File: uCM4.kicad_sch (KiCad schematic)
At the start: 77 parts, among them IC1 MAX17048G+, J10 USB_C_Receptacle, J12 Conn_02x08_Odd_Even, J13 Conn_02x07_Odd_Even, J2 Micro_SD_Card_Det, J4 Conn_01x04, J5 DummyJ, J6 DummyJ, J8 Camera 0, J9 Camera 1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

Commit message: Routing
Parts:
- removed TP1, TP3, TP4, TP5, TP6, TP7, TP9: TestPoint, TestPoint:TestPoint_Pad_D1.0mm, symbol Connector:TestPoint
- removed U3: TPD4EUSB30DQAR, Package_SON:USON-10_2.5x1.0mm_P0.5mm, symbol Power_Protection:TPD4EUSB30
- added U5: TPD2EUSB30, Package_TO_SOT_SMD:Texas_DRT-3, symbol Power_Protection:TPD2EUSB30
- J2: footprint CM4:SDCARD_MOLEX_503398-1892 -> Connector_Card:microSD_HC_Hirose_DM3AT-SF-PEJM5
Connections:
- net GND: now also U5.3 (GND)
- net USB_N: now also U5.2 (D-)
- net USB_P: now also U5.1 (D+)
- net ENV_SEL: no longer names the net of Module1.37 (GPIO7)
- no-connect marks 97 -> 96
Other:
- note added: "Might be worth double checking pins one more time."
- note added: "Would be good to double check if this will work as intended."
- moved on the sheet: TP10, TP11, TP12, TP2, TP8

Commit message: Updating LCSC numbers.
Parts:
- C1, C11: LCSC Part # (none) -> C14445
- C2, C3: LCSC Part # (none) -> C1525
- C5: LCSC Part # (none) -> C117956
- C8, C9: LCSC Part # (none) -> C19702
- D1: LCSC Part # (none) -> C181863; LCSC# C181863 -> (none)
- D2: LCSC Part # (none) -> C72043; LCSC# C72043 -> (none)
- D3: LCSC Part # (none) -> C72043
- D8: LCSC Part # (none) -> C727059
- J10: LCSC (none) -> C5184243
- J2: LCSC Part # (none) -> C428492
- J8, J9: LCSC Part # (none) -> C597981
- L1: LCSC Part # (none) -> C19191626
- Module1: LCSC Part # (none) -> C424649; LCSC# C424649 -> (none)
- R10, R13, R15: LCSC Part # (none) -> C21190; LCSC# C21190 -> (none)
- R12, R14: LCSC Part # (none) -> C60490
- R16: LCSC Part # (none) -> C269673
- R29: LCSC Part # (none) -> C25752
- R8, R9: LCSC Part # (none) -> C25905
- SW1: LCSC Part # (none) -> C221907; LCSC# C221911 -> (none)
- SW3: LCSC Part # (none) -> C221907
- U1: LCSC Part # (none) -> C93216
- U18: LCSC Part # (none) -> C250547
- U2: LCSC Part # (none) -> C7829; LCSC# C7829 -> (none)
- U4: LCSC Part # (none) -> C915088
- U5: LCSC Part # (none) -> C3040102
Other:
- note added: "Still need to fix distances for diff pairs"

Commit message: Tuning differential traces and changing some footprints
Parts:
- J2: footprint Connector_Card:microSD_HC_Hirose_DM3AT-SF-PEJM5 -> CM4:SDCARD_MOLEX_503398-1892
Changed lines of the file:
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@@
 			)
 		)
-		(property "Footprint" "Connector_Card:microSD_HC_Hirose_DM3AT-SF-PEJM5"
+		(property "Footprint" "CM4:SDCARD_MOLEX_503398-1892"
 			(at 326.39 38.1 0)
 			(effects

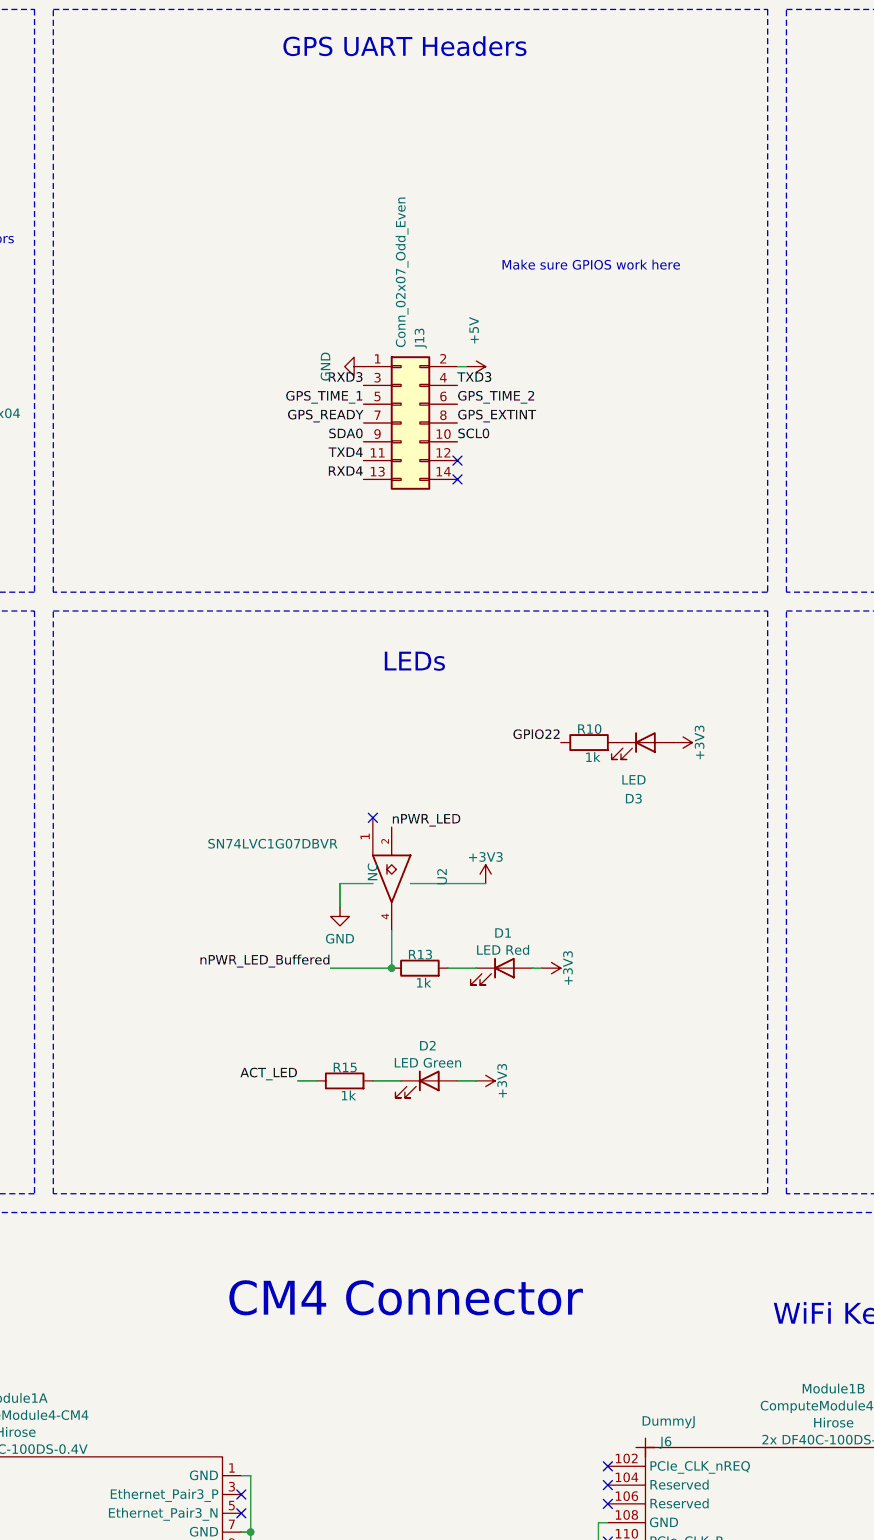
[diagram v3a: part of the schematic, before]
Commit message: Finalized LCSC selections
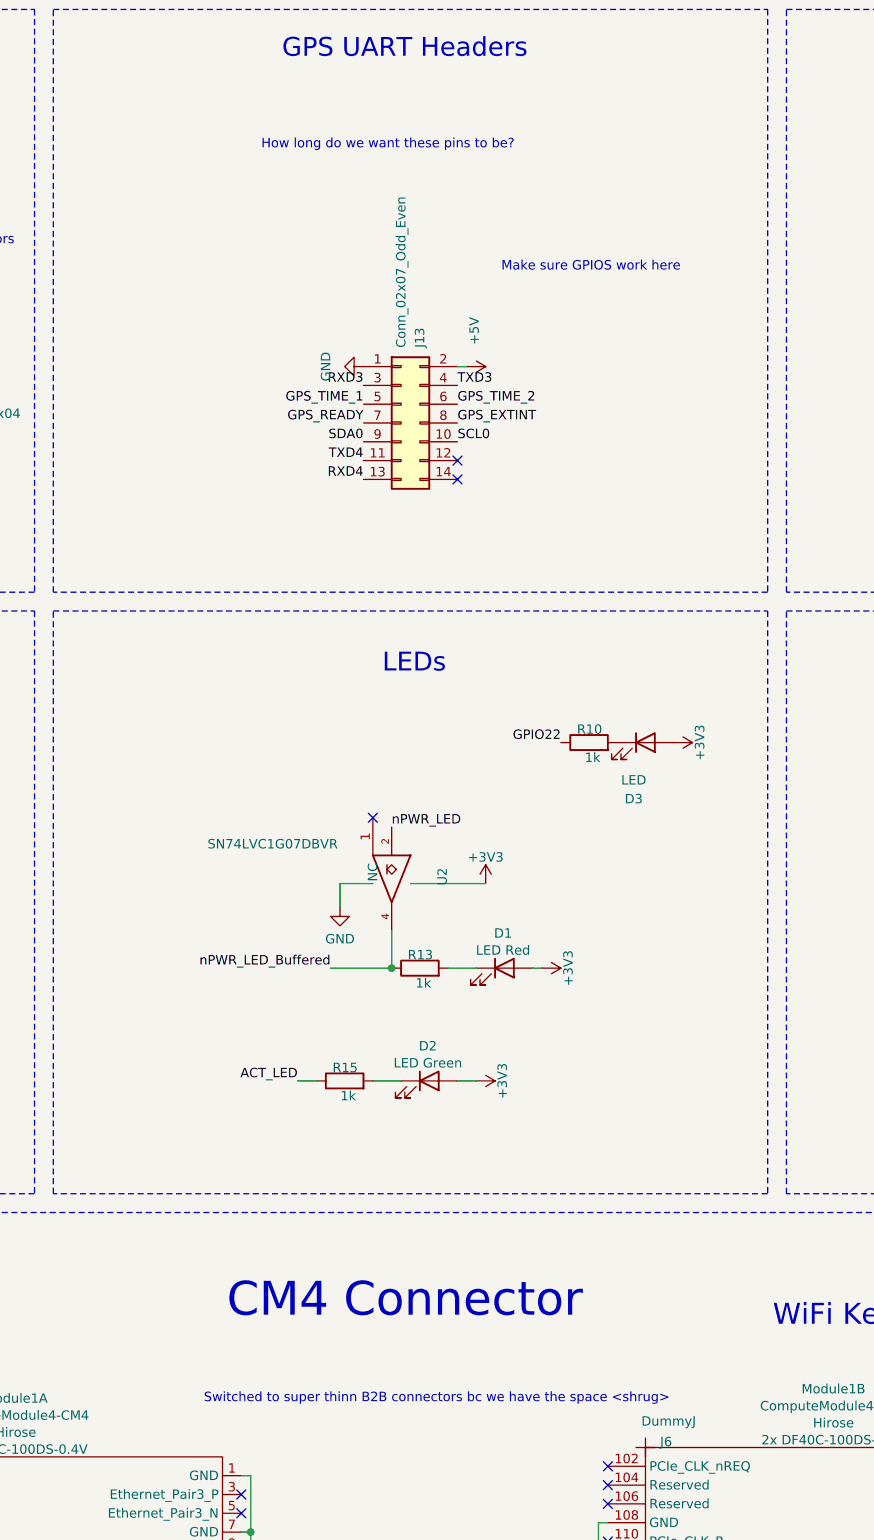
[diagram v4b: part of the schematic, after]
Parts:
- BT1: Digikey (none) -> https://www.digikey.com/en/products/detail/jst-sales-americ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; LCSC Part # (none) -> C2763702
- C13: LCSC Part # (none) -> C1525
- C4, C6, C7: LCSC Part # (none) -> C12891
- D6: LCSC Part # (none) -> C72043
- D7: LCSC Part # (none) -> C181863
- IC1: LCSC Part # (none) -> C2682616
- J12: LCSC Part # (none) -> C22239874
- J13: LCSC Part # (none) -> C180404
- J4: LCSC Part # (none) -> C160390
- Module1: LCSC Part # C424649 -> C597931
- Q2: LCSC Part # (none) -> C15127
- R16: LCSC Part # C269673 -> C852472
- R19: LCSC Part # (none) -> C190095
- R21: LCSC Part # (none) -> C852472
- R22: LCSC Part # (none) -> C25882
- R24: LCSC Part # (none) -> C21190
- R6, R7: LCSC Part # (none) -> C60488
- S1, S2: LCSC Part # (none) -> C221661
- SW4: LCSC Part # (none) -> C221841
- U6: LCSC Part # (none) -> C725791
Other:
- note added: "How long do we want these pins to be?"
- note added: "Switched to super thinn B2B connectors bc we have the space <shrug>"
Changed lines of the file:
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@@
 		)
 	)
+	(text "Switched to super thinn B2B connectors bc we have the space <shrug>"
+		(exclude_from_sim no)
+		(at 167.386 205.486 0)
+		(effects
+			(font
+				(size 1.27 1.27)
+				(color 255 2 9 1)
+			)
+		)
+	)
 	(text "Test Points"
 		(exclude_from_sim no)
@@
 		)
 	)
+	(text "How long do we want these pins to be?"
+		(exclude_from_sim no)
+		(at 160.782 36.068 0)
+		(effects
+			(font
+				(size 1.27 1.27)
+				(color 255 16 55 1)
+			)
+		)
+	)
 	(text "UART extension pins (FDTI compatible)"
 		(exclude_from_sim no)
@@
 			)
 		)
+		(property "LCSC Part #" "C60488"
+			(at 44.45 85.09 0)
+			(effects
+				(font
+					(size 1.27 1.27)
+				)
+				(hide yes)
+			)
+		)
 		(pin "1"
 		)
@@
 			)
 		)
+		(property "LCSC Part #" "C60488"
+			(at 36.83 85.09 0)
+			(effects
+				(font
+					(size 1.27 1.27)
+				)
+				(hide yes)
+			)
+		)
 		(pin "1"
 		)
@@
 			)
 		)
+		(property "LCSC Part #" "C21190"
+			(at 429.26 157.48 90)
+			(effects
+				(font
+					(size 1.27 1.27)
+				)
+				(hide yes)
+			)
+		)
 		(pin "2"
 		)
@@
 			)
 		)
+		(property "LCSC Part #" "C1525"
+			(at 448.31 124.46 90)
+			(effects
+				(font
+					(size 1.27 1.27)
+				)
+				(hide yes)
+			)
+		)
 		(pin "1"
 		)
@@
 			)
 		)
-		(property "LCSC Part #" "C424649"
+		(property "LCSC Part #" "C597931"
 			(at 81.28 275.59 0)
 			(effects
@@
 			)
 		)
+		(property "LCSC Part #" "C15127"
+			(at 487.68 152.4 90)
+			(effects
+				(font
+					(size 1.27 1.27)
+				)
+				(hide yes)
+			)
+		)
 		(pin "3"
 		)
@@
 			)
 		)
+		(property "LCSC Part #" "C25882"
+			(at 464.82 160.02 90)
+			(effects
+				(font
+					(size 1.27 1.27)
+				)
+				(hide yes)
+			)
+		)
 		(pin "2"
 		)
@@
 			)
 		)
+		(property "LCSC Part #" "C181863"
+			(at 436.88 154.94 0)
+			(effects
+				(font
+					(size 1.27 1.27)
+				)
+				(hide yes)
+			)
+		)
 		(pin "1"
 		)
@@
 			)
 		)
+		(property "LCSC Part #" "C725791"
+			(at 450.85 157.48 0)
+			(effects
+				(font
+					(size 1.27 1.27)
+				)
+				(hide yes)
+			)
+		)
 		(pin "5"
 		)
@@
 			)
 		)
+		(property "LCSC Part #" "C160390"
+			(at 97.79 69.85 0)
+			(effects
+				(font
+					(size 1.27 1.27)
+				)
+				(hide yes)
+			)
+		)
 		(pin "3"
 		)
@@
 			)
 		)
+		(property "LCSC Part #" "C221661"
+			(at 171.45 335.28 0)
+			(effects
+				(font
+					(size 1.27 1.27)
+				)
+				(hide yes)
+			)
+		)
 		(pin "1"
 		)
@@
 			)
 		)
+		(property "LCSC Part #" "C180404"
+			(at 162.56 73.66 90)
+			(effects
+				(font
+					(size 1.27 1.27)
+				)
+				(hide yes)
+			)
+		)
 		(pin "14"
 		)
@@
 			)
 		)
+		(property "LCSC Part #" "C221841"
+			(at 157.48 353.06 0)
+			(effects
+				(font
+					(size 1.27 1.27)
+				)
+				(hide yes)
+			)
+		)
 		(pin "3"
 		)
@@
 			)
 		)
-		(property "LCSC Part #" "C424649"
+		(property "LCSC Part #" "C597931"
 			(at 113.03 271.78 0)
 			(effects
@@
 			)
 		)
+		(property "LCSC Part #" "C12891"
+			(at 393.7 132.08 0)
+			(effects
+				(font
+					(size 1.27 1.27)
+				)
+				(hide yes)
+			)
+		)
 		(pin "2"
 		)
@@
 			)
 		)
+		(property "LCSC Part #" "C12891"
+			(at 393.7 120.65 0)
+			(effects
+				(font
+					(size 1.27 1.27)
+				)
+				(hide yes)
+			)
+		)
 		(pin "2"
 		)
@@
 			)
 		)
+		(property "LCSC Part #" "C221661"
+			(at 276.86 217.17 0)
+			(effects
+				(font
+					(size 1.27 1.27)
+				)
+				(hide yes)
+			)
+		)
 		(pin "1"
 		)
@@
 			)
 		)
-		(property "LCSC Part #" "C269673"
+		(property "LCSC Part #" "C852472"
 			(at 386.08 154.94 0)
 			(effects
@@
 			)
 		)
+		(property "LCSC Part #" "C2682616"
+			(at 458.47 116.84 0)
+			(effects
+				(font
+					(size 1.27 1.27)
+				)
+				(hide yes)
+			)
+		)
 		(pin "5"
 		)
@@
 			)
 		)
+		(property "LCSC Part #" "C852472"
+			(at 487.68 161.29 0)
+			(effects
+				(font
+					(size 1.27 1.27)
+				)
+				(hide yes)
+			)
+		)
 		(pin "2"
 		)
@@
 			)
 		)
+		(property "LCSC Part #" "C72043"
+			(at 436.88 160.02 0)
+			(effects
+				(font
+					(size 1.27 1.27)
+				)
+				(hide yes)
+			)
+		)
 		(pin "1"
 		)
@@
 			)
 		)
+		(property "LCSC Part #" "C190095"
+			(at 393.7 151.13 90)
+			(effects
+				(font
+					(size 1.27 1.27)
+				)
+				(hide yes)
+			)
+		)
 		(pin "1"
 		)
@@
 			)
 		)
+		(property "LCSC Part #" "C12891"
+			(at 393.7 143.51 0)
+			(effects
+				(font
+					(size 1.27 1.27)
+				)
+				(hide yes)
+			)
+		)
 		(pin "2"
 		)
@@
 			)
 		)
+		(property "LCSC Part #" "C22239874"
+			(at 48.26 58.42 0)
+			(effects
+				(font
+					(size 1.27 1.27)
+				)
+				(hide yes)
+			)
+		)
 		(pin "4"
 		)
@@
 				(hide yes)
 			)
+		)
+		(property "Digikey" "https://www.digikey.com/en/products/detail/jst-sales-america-inc/B2B-PH-SM4-TB/926641"
+			(at 425.45 128.27 0)
+			(effects
+				(font
+					(size 1.27 1.27)
+				)
+				(hide yes)
+			)
+		)
+		(property "LCSC Part #" "C2763702"
+			(at 425.45 128.27 0)
+			(effects
+				(font
+					(size 1.27 1.27)
+				)
+				(hide yes)
+			)

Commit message: Prepping for production.
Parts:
- C11: LCSC Part # C14445 -> C77177
- C5: value 10u -> 10uF; LCSC Part # C117956 -> C19702
- D1, D7: LCSC Part # C181863 -> C264407
- D2, D3, D6: LCSC Part # C72043 -> C5123485
- J12: LCSC Part # C22239874 -> C32713288
- J13: LCSC Part # C180404 -> C3294465
- R1: LCSC Part # (none) -> C22962; LCSC# C22962 -> (none)
- R10, R13, R15, R24: LCSC Part # C21190 -> C106235
- R2, R4: LCSC Part # (none) -> C106231; LCSC# C22962 -> (none)
- R20: LCSC Part # (none) -> C21189; LCSC# C21189 -> (none)
- R23, R3: LCSC Part # (none) -> C106231; LCSC# C21189 -> (none)
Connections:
- net GND: now also U6.2 (GND)
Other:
- note added: "Part not correct?"
- note added: "Wrong SMD part size!"
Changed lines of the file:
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@@
 		)
 	)
+	(text "Wrong SMD part size!"
+		(exclude_from_sim no)
+		(at 147.066 44.958 0)
+		(effects
+			(font
+				(size 1.27 1.27)
+				(color 255 0 224 1)
+			)
+		)
+	)
 	(text "Stemma/QUIIC Connector for external sensors"
 		(exclude_from_sim no)
@@
 		)
 	)
+	(text "Part not correct?"
+		(exclude_from_sim no)
+		(at 44.958 32.258 0)
+		(effects
+			(font
+				(size 1.27 1.27)
+				(color 255 0 224 1)
+			)
+		)
+	)
 	(text "Camera Connectors"
 		(exclude_from_sim no)
@@
 			)
 		)
-		(property "Value" "10u"
+		(property "Value" "10uF"
 			(at 232.791 53.213 0)
 			(effects
@@
 			)
 		)
-		(property "LCSC Part #" "C117956"
+		(property "LCSC Part #" "C19702"
 			(at 229.87 52.07 0)
 			(effects
@@
 			)
 		)
-		(property "LCSC Part #" "C21190"
+		(property "LCSC Part #" "C106235"
 			(at 429.26 157.48 90)
 			(effects
@@
 			)
 		)
-		(property "LCSC#" "C22962"
+		(property "LCSC Part #" "C106231"
 			(at 60.96 312.42 0)
 			(effects
@@
 			)
 		)
-		(property "LCSC Part #" "C21190"
+		(property "LCSC Part #" "C106235"
 			(at 187.96 116.84 0)
 			(effects
@@
 			)
 		)
-		(property "LCSC Part #" "C181863"
+		(property "LCSC Part #" "C264407"
 			(at 176.53 147.32 0)
 			(effects
@@
 			)
 		)
-		(property "LCSC#" "C22962"
+		(property "LCSC Part #" "C22962"
 			(at 54.61 351.79 0)
 			(effects
@@
 			)
 		)
-		(property "LCSC#" "C21189"
+		(property "LCSC Part #" "C106231"
 			(at 83.82 69.85 0)
 			(effects
@@
 			)
 		)
-		(property "LCSC Part #" "C181863"
+		(property "LCSC Part #" "C264407"
 			(at 436.88 154.94 0)
 			(effects
@@
 	)
 	(symbol
+		(lib_name "GND_11")
+		(lib_id "power:GND")
+		(at 450.85 165.1 0)
+		(unit 1)
+		(exclude_from_sim no)
+		(in_bom yes)
+		(on_board yes)
+		(dnp no)
+		(fields_autoplaced yes)
+		(property "Reference" "#PWR018"
+			(at 450.85 171.45 0)
+			(effects
+				(font
+					(size 1.27 1.27)
+				)
+				(hide yes)
+			)
+		)
+		(property "Value" "GND"
+			(at 450.85 170.18 0)
+			(effects
+				(font
+					(size 1.27 1.27)
+				)
+			)
+		)
+		(property "Footprint" ""
+			(at 450.85 165.1 0)
+			(effects
+				(font
+					(size 1.27 1.27)
+				)
+				(hide yes)
+			)
+		)
+		(property "Datasheet" ""
+			(at 450.85 165.1 0)
+			(effects
+				(font
+					(size 1.27 1.27)
+				)
+				(hide yes)
+			)
+		)
+		(property "Description" "Power symbol creates a global label with name \"GND\" , ground"
+			(at 450.85 165.1 0)
+			(effects
+				(font
+					(size 1.27 1.27)
+				)
+				(hide yes)
+			)
+		)
+		(pin "1"
+		)
+		(instances
+			(project "uCM4"
+				(path "/ab308ddb-f5b4-4376-8062-4d719b3e690f"
+					(reference "#PWR018")
+					(unit 1)
+				)
+			)
+		)
+	)
+	(symbol
 		(lib_name "GND_5")
 		(lib_id "power:GND")
@@
 			)
 		)
-		(property "LCSC#" "C21189"
+		(property "LCSC Part #" "C21189"
 			(at 34.29 55.88 0)
 			(effects
@@
 			)
 		)
-		(property "LCSC Part #" "C180404"
+		(property "LCSC Part #" "C3294465"
 			(at 162.56 73.66 90)
 			(effects
@@
 			)
 		)
-		(property "LCSC#" "C22962"
+		(property "LCSC Part #" "C106231"
 			(at 60.96 309.88 0)
 			(effects
@@
 			)
 		)
-		(property "LCSC#" "C21189"
+		(property "LCSC Part #" "C106231"
 			(at 63.5 237.49 0)
 			(effects
@@
 			)
 		)
-		(property "LCSC Part #" "C72043"
+		(property "LCSC Part #" "C5123485"
 			(at 195.58 116.84 0)
 			(effects
@@
 			)
 		)
-		(property "LCSC Part #" "C21190"
+		(property "LCSC Part #" "C106235"
 			(at 165.1 147.32 0)
 			(effects
@@
 			)
 		)
-		(property "LCSC Part #" "C72043"
+		(property "LCSC Part #" "C5123485"
 			(at 166.37 162.56 0)
 			(effects
@@
 			)
 		)
-		(property "LCSC Part #" "C72043"
+		(property "LCSC Part #" "C5123485"
 			(at 436.88 160.02 0)
 			(effects
@@
 			)
 		)
-		(property "LCSC Part #" "C14445"
+		(property "LCSC Part #" "C77177"
 			(at 378.46 144.78 90)
 			(effects
@@
 			)
 		)
-		(property "LCSC Part #" "C21190"
+		(property "LCSC Part #" "C106235"
 			(at 154.94 162.56 0)
 			(effects
@@
 			)
 		)
-		(property "LCSC Part #" "C22239874"
+		(property "LCSC Part #" "C32713288"
 			(at 48.26 58.42 0)
 			(effects

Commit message: Updated comments.
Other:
- note removed: "Part not correct?"
- note removed: "Wrong SMD part size!"
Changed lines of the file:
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@@
-		)
-	)
-	(text "Wrong SMD part size!"
-		(exclude_from_sim no)
-		(at 147.066 44.958 0)
-		(effects
-			(font
-				(size 1.27 1.27)
-				(color 255 0 224 1)
-			)
 		)
 	)
@@
 			)
 		)
-	)
-	(text "Part not correct?"
-		(exclude_from_sim no)
-		(at 44.958 32.258 0)
-		(effects
-			(font
-				(size 1.27 1.27)
-				(color 255 0 224 1)
-			)
-		)

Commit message: Adding github issues. Almost completed in schematic.
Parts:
- removed C11: 105pF, Capacitor_SMD:C_0402_1005Metric, symbol Device:C
- added R11, R5: 2.2K 1%, Resistor_SMD:R_0402_1005Metric, symbol Device:R
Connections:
- net +3.3v is gone; now on net +3V3: R17.1, R29.1, U18.5 (IN)
- net GPIO_VREF: now also R11.2, R5.2
- net RXD5: now also U1.20 (COM0); no longer U1.19 (COM1)
- net SCL0: now also J9.20 (Pin_20); no longer J8.20 (Pin_20)
- net SCL1: now also J8.20 (Pin_20), Module1.35 (ID_SC); no longer J4.4 (Pin_4), J9.20 (Pin_20), Module1.56 (GPIO3)
- net SDA0: now also J9.21 (Pin_21); no longer J8.21 (Pin_21)
- net SDA1: now also J8.21 (Pin_21), Module1.36 (ID_SD); no longer J4.3 (Pin_3), J9.21 (Pin_21), Module1.58 (GPIO2)
- net TXD5: now also U1.19 (COM1); no longer U1.20 (COM0)
- new net SCL3: J4.3 (Pin_3), Module1.56 (GPIO3), R5.1
- new net SDA3: J4.4 (Pin_4), Module1.58 (GPIO2), R11.1
- no-connect marks 96 -> 94
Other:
- note added: "I2C0 has internal pullups."
- note added: "I2C: 0x36/0x6C/0x6D most likely"
- note added: "I2C: 0x84 most likely"
- note added: "Issue #11: (FIXED) Feedforward cap removed"
- note added: "Issue #15: Options Replace with TPS61230A? Replace with https://www.ti.com/lit/ds/symlink/tps61089.pdf?ts=1768526433213&ref_url=https%253A%252F%252Feu.mouser.com%252F Implement 1.8V UVLO? https://www.ti.com/lit/an/slvaen1a/slvaen1a.pdf?ts=1768525897594&ref_url=https%253A%252F%252Fclaude.ai%252F"
- note added: "Issue #1: (FIXED, CONFIRM) Switched I2C connecitons"
- note added: "Issue #2: (FIXED, CONFIRM) Switched I2C connecitons."
- note added: "Issue #4: (FIXED) swap TX/RX pins"
- note added: "Issue #5: (FIXED) +3.3v replaced with 3V3"
- note added: "Issue #7: Fix R19 value"
- note removed: "<-- Check if these switches make sense -->"
- note removed: "Does this switch make sense?"
- note removed: "Feedforward cap"
- note removed: "I2C 1 Requires External Pullups (not true for I2C0)"
- note removed: "Still need to fix distances for diff pairs"
- note removed: "Switched to super thinn B2B connectors bc we have the space <shrug>"
- note removed: "Would be good to double check if this will work as intended."
